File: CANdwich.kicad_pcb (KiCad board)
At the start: 2 copper layers, 43 parts, among them J1 DE9_Receptacle, J2 USB_C_Receptacle_USB2.0, J3 Conn_02x05_Odd_Even, J4 Conn_01x04_Socket, U1 AP2127K-3.3, U2 STM32F072CBT6, U3 SN6505BDBV, U5 AP2204RA-5.0, U6 ISO1050DUB, Y1 16MHz

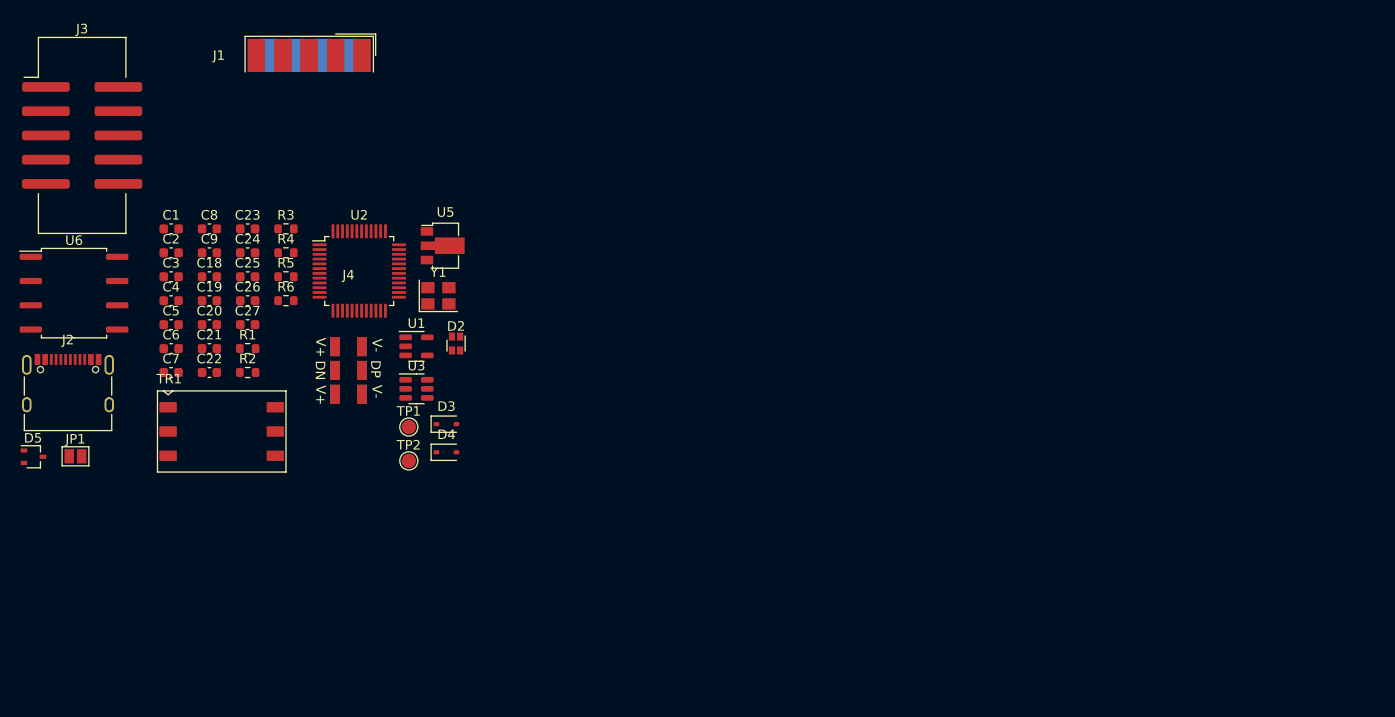
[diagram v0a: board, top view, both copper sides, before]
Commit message: Placement in KICAD V7.0.5
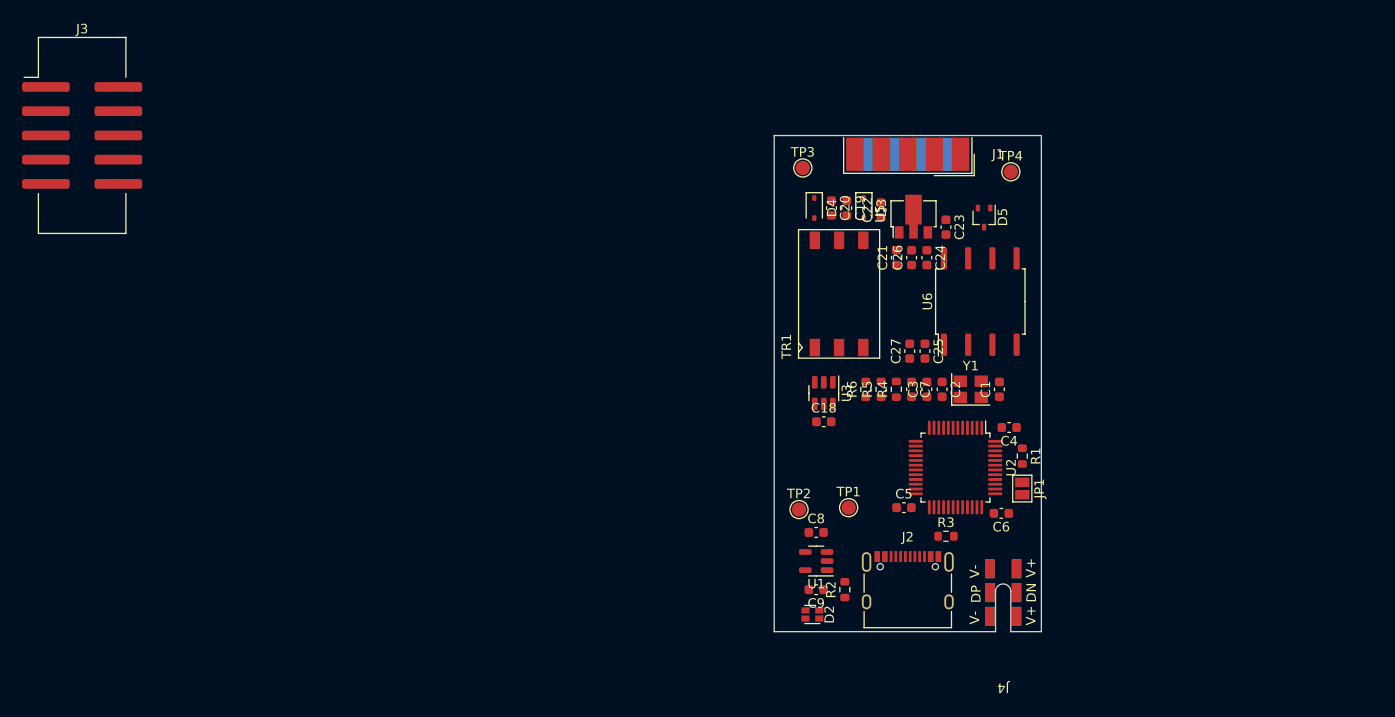
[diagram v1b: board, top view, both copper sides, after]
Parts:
- added TP3: TestPoint, TestPoint:TestPoint_Pad_D1.5mm, F.Cu at (119.0, 60.4)
- added TP4: TestPoint, TestPoint:TestPoint_Pad_D1.5mm, F.Cu at (140.8, 60.8)
- J1: footprint Connector_Dsub:DSUB-9_Female_EdgeMount_P2.77mm -> Connector_Dsub:DSUB-9_Male_EdgeMount_P2.77mm
- moved D5 102.7 mm to (138.0, 65.6), turned to -90 degrees
- moved JP1 99.3 mm to (142.0, 94.0), turned to -90 degrees
- moved U6 95.0 mm to (137.6, 74.4), turned to 90 degrees
- moved J2 90.4 mm to (130.0, 104.8)
- moved C4 88.8 mm to (140.6, 87.6), turned to 180 degrees
- moved C6 88.7 mm to (139.8, 96.6), turned to 180 degrees
- moved C1 88.4 mm to (139.6, 83.6), turned to 90 degrees
- moved C2 82.1 mm to (133.6, 83.6), turned to -90 degrees
- moved R1 82.0 mm to (142.0, 90.6), turned to -90 degrees
- moved C3 80.1 mm to (132.0, 83.6), turned to 90 degrees
- moved C5 79.2 mm to (129.6, 96.0)
- moved C7 77.6 mm to (130.4, 83.6), turned to -90 degrees
- moved R3 76.3 mm to (134.0, 99.0)
- moved J4 75.4 mm to (140.0, 108.9), turned to 180 degrees
- moved C23 73.2 mm to (134.0, 66.6), turned to -90 degrees
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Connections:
- TR1 pad 1: Net-(U3-D1) -> Net-(U3-D2)
- TR1 pad 3: Net-(U3-D2) -> Net-(U3-D1)
- TR1 pad 4: Net-(D4-A) -> Net-(D3-A)
- TR1 pad 6: Net-(D3-A) -> Net-(D4-A)
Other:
- board outline added: 28 x 52 mm

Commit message: Snapshot for layout
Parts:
- removed C21: 1u, Capacitor_SMD:C_0603_1608Metric
- removed J3: Conn_02x05_Odd_Even, Connector_IDC:IDC-Header_2x05_P2.54mm_Vertical_SMD
- removed JP1: Jumper_2_Open, Jumper:SolderJumper-2_P1.3mm_Open_Pad1.0x1.5mm
- added R7: 150, Resistor_SMD:R_0603_1608Metric, F.Cu at (135.6, 97.6)
- added TP5: TestPoint, TestPoint:TestPoint_Pad_D1.5mm, F.Cu at (140.0, 95.4)
- added TP6: TestPoint, TestPoint:TestPoint_Pad_D1.5mm, F.Cu at (140.0, 97.9)
- added TP7: TestPoint, TestPoint:TestPoint_Pad_D1.5mm, F.Cu at (140.0, 92.9)
- added TP8: TestPoint, TestPoint:TestPoint_Pad_D1.5mm, F.Cu at (139.0, 69.9)
- added TP9: TestPoint, TestPoint:TestPoint_Pad_D1.5mm, F.Cu at (140.0, 90.4)
- R4, R5, R6: value 121 -> 150
- Y1: footprint Crystal:Crystal_SMD_3225-4Pin_3.2x2.5mm -> Crystal:Crystal_SMD_2520-4Pin_2.5x2.0mm
- moved R6 22.0 mm to (119.4, 104.7)
- moved R1 7.50 mm to (136.0, 95.1)
- moved C8 7.25 mm to (123.8, 105.0), turned to 90 degrees
- moved C4 6.72 mm to (134.8, 91.0)
- moved U2 6.36 mm to (129.5, 95.0)
- moved C5 6.13 mm to (123.5, 96.6), turned to -90 degrees
- moved TP3 5.85 mm to (121.0, 65.9)
- moved D5 5.76 mm to (136.2, 71.0)
- moved C6 5.73 mm to (134.8, 99.4)
- moved C1 5.66 mm to (135.6, 87.6)
- moved TP4 5.41 mm to (139.0, 65.9)
- moved R2 5.36 mm to (124.2, 99.3), turned to 180 degrees
- moved Y1 5.32 mm to (133.1, 87.6)
- moved D4 5.01 mm to (121.0, 69.5)
- moved C2 5.00 mm to (130.6, 87.6)
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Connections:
- net /USB_DM renamed /USB_D-
- net /USB_DP renamed /USB_D+
- net Net-(U2-PF0) renamed /clk_P
- net Net-(U2-PF1) renamed /clk_N
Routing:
- net Net-(D2-RK): track 0.00 -> 31.8 mm, vias 0 -> 2
- net Net-(D2-GK): track 0.00 -> 28.2 mm, vias 0 -> 2
- net VBUS: track 0.00 -> 24.9 mm, vias 0 -> 13
- net /USB_D-: track 0.00 -> 24.1 mm, vias 0 -> 2
- net /USB_D+: track 0.00 -> 21.9 mm, vias 0 -> 2
- net /CAN_RX: track 0.00 -> 18.8 mm
- net +5VD: track 0.00 -> 17.9 mm, vias 0 -> 2
- net /nRST: track 0.00 -> 14.9 mm, vias 0 -> 2
- net /SWDIO: track 0.00 -> 14.3 mm, vias 0 -> 2
- net /CAN_TX: track 0.00 -> 12.4 mm
- net /CANH: track 0.00 -> 11.8 mm, vias 0 -> 1
- net /CANL: track 0.00 -> 11.8 mm
- net Earth: track 0.00 -> 11.2 mm, vias 0 -> 44
- net /SWCLK: track 0.00 -> 9.21 mm, vias 0 -> 2
- net VD3V3: track 0.00 -> 8.86 mm
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- added copper zone on B.Cu, net +12V
- added copper zone on F.Cu, net +12V
- added copper zone on B.Cu, net Earth
- added copper zone on F.Cu, net Earth
- added copper zone on B.Cu, net GNDA
- added copper zone on F.Cu, net GNDA
- added copper zone on B.Cu, net VBUS
- added copper zone on F.Cu, net VBUS
- added copper zone on F.Cu, net VD3V3
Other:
- board size 28 x 52 mm -> 26 x 46 mm

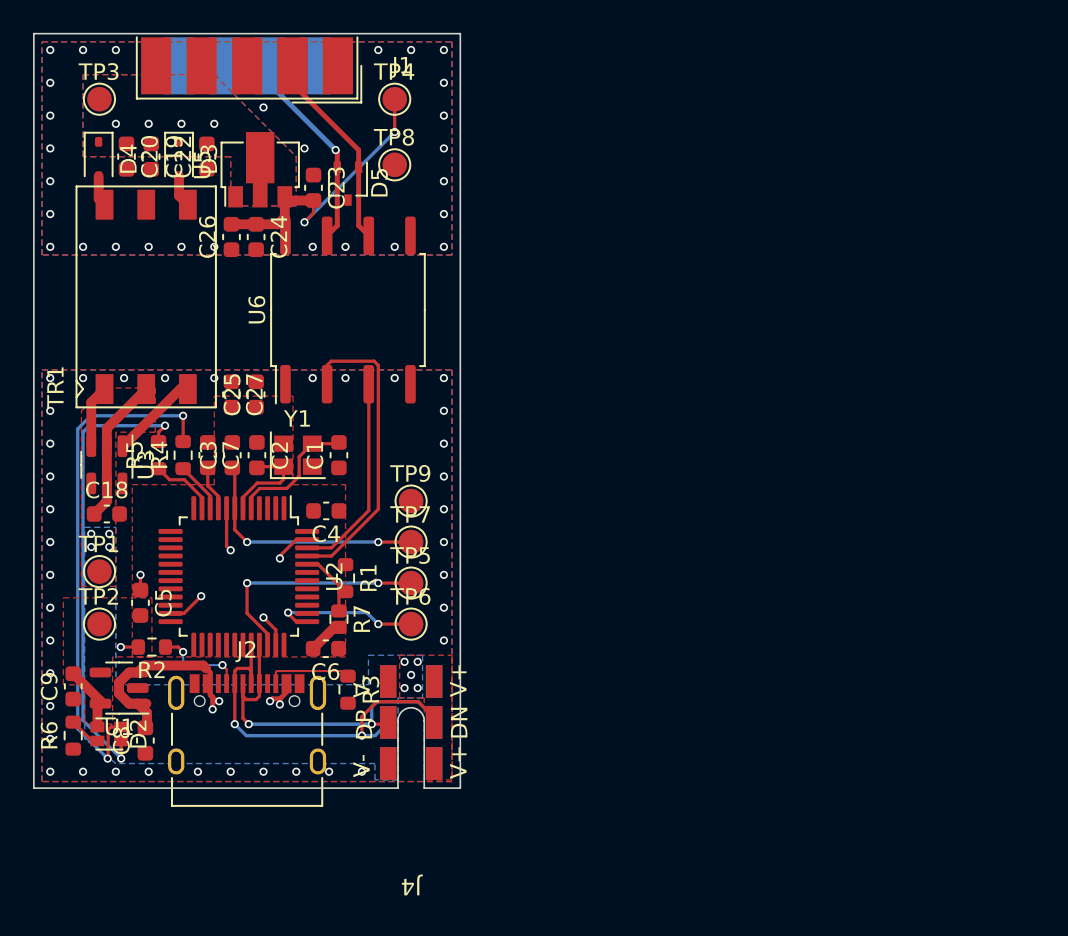
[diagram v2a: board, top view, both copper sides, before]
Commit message: resize edge.cuts
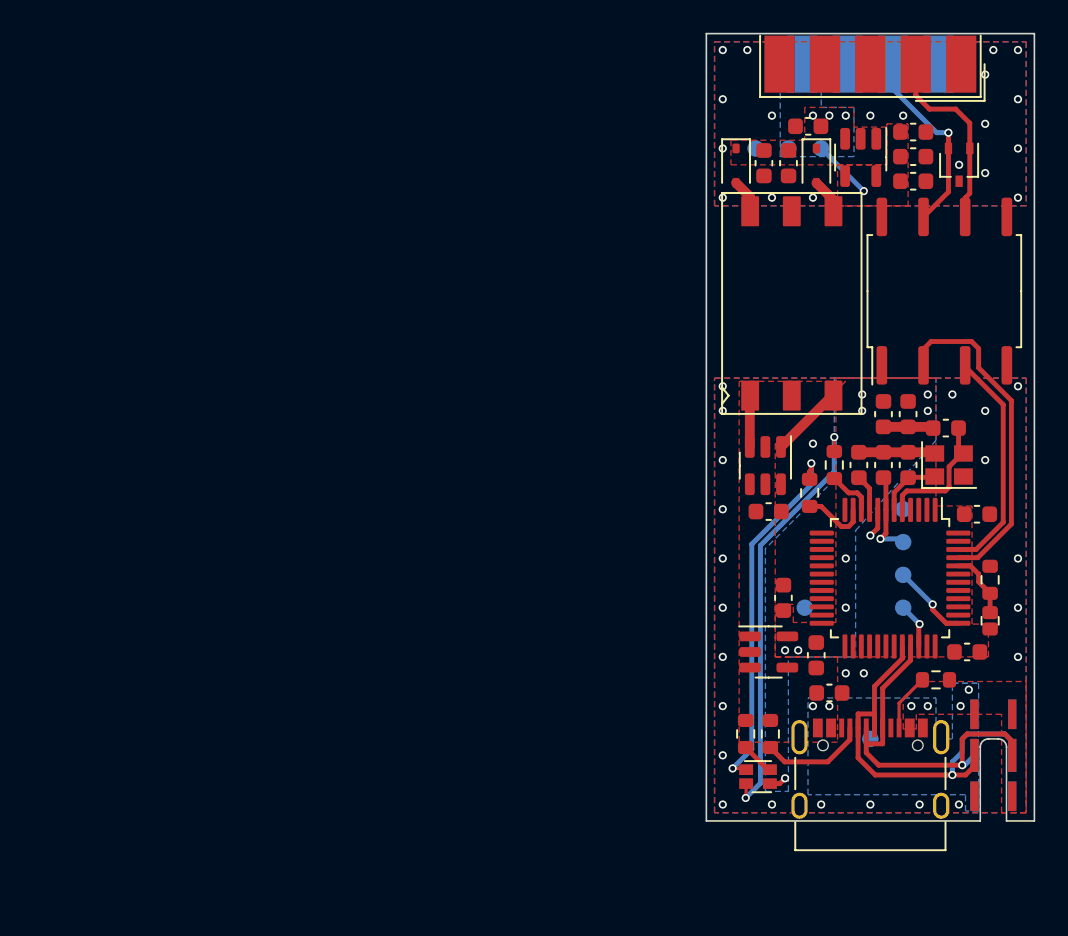
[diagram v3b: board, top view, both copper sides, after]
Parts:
- removed U5: AP2204RA-5.0, Package_TO_SOT_SMD:SOT-89-3
- added G***: LOGO, LOGO, B.Cu at (230.3, 72.2)
- added U4: AP2204K-5.0TRG1, Package_TO_SOT_SMD:SOT-23-5, F.Cu at (167.4, 69.5)
- J4: moved to B.Cu
- TP1, TP2, TP3, TP4, TP5, TP6, TP7, TP8, TP9: footprint TestPoint:TestPoint_Pad_D1.5mm -> TestPoint:TestPoint_Pad_D1.0mm; moved to B.Cu
- moved TP1 48.1 mm to (168.0, 104.9), turned to 180 degrees
- moved C9 43.6 mm to (162.7, 96.3), turned to -90 degrees
- moved TP2 43.0 mm to (164.0, 96.9), turned to 180 degrees
- moved TP3 42.1 mm to (163.0, 68.9), turned to 180 degrees
- moved C26 41.8 mm to (170.6, 69.4), turned to 180 degrees
- moved C8 41.8 mm to (165.5, 102.1), turned to 180 degrees
- moved C5 41.3 mm to (164.7, 99.8), turned to 90 degrees
- moved C27 41.3 mm to (170.3, 85.1), turned to 90 degrees
- moved R6 41.0 mm to (160.4, 104.6), turned to -90 degrees
- moved C24 40.6 mm to (170.6, 67.9), turned to 0 degrees
- moved C18 40.4 mm to (161.8, 91.0)
- moved U3 40.2 mm to (161.6, 88.2)
- moved R5 39.8 mm to (164.3, 89.9)
- moved C2 39.7 mm to (170.3, 88.2)
- moved C3 39.7 mm to (168.8, 88.2)
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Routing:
- net VBUS: track 24.9 -> 0.00 mm, vias 13 -> 6
- net +5VD: track 17.9 -> 3.68 mm, vias 2 -> 1
- net /SWDIO: track 14.3 -> 2.80 mm, vias 2 -> 1
- net /nRST: track 14.9 -> 5.40 mm, vias 2 -> 1
- net Net-(D2-RK): track 31.8 -> 26.0 mm
- net Net-(D2-GK): track 28.2 -> 22.5 mm
- net VD3V3: track 8.86 -> 3.29 mm, vias 0 -> 9
- net /SWCLK: track 9.21 -> 4.77 mm, vias 2 -> 1
- net /clk_N: track 6.03 -> 3.92 mm
- net Net-(J2-CC2): track 5.26 -> 3.52 mm
- net Earth: track 11.2 -> 9.46 mm, vias 44 -> 26
- net /CAN_RX: track 18.8 -> 20.3 mm
- net /CAN_TX: track 12.4 -> 14.0 mm
- net /USB_D-: track 24.1 -> 25.3 mm, vias 2 -> 1
- net Net-(J2-CC1): track 5.52 -> 6.49 mm, vias 2 -> 0
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- added copper zone on F.Cu, net +5VD
- added copper zone on B.Cu, net VD3V3
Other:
- board size 26 x 46 mm -> 20 x 48 mm

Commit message: V1.0 Generate external enclosure
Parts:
- moved G*** 63.9 mm to (168.0, 86.2)

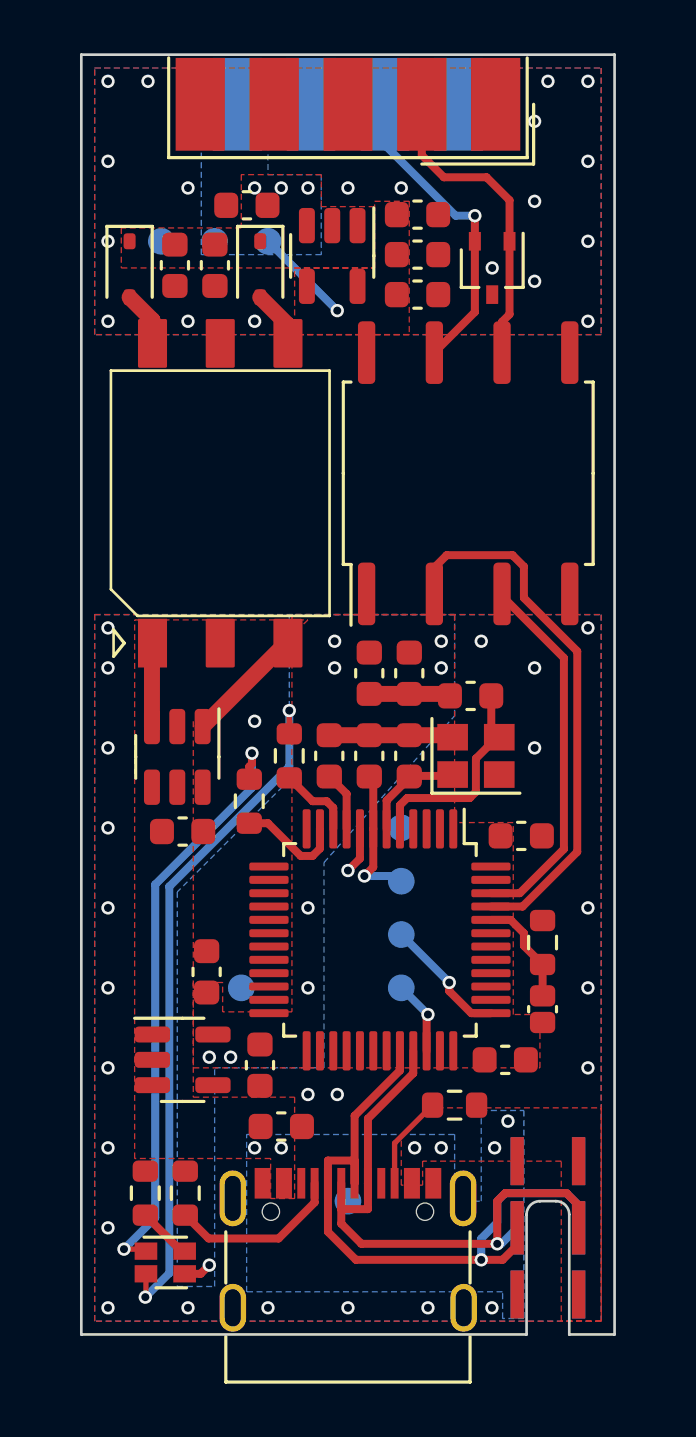
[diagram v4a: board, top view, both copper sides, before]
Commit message: Change USB edge connection interface
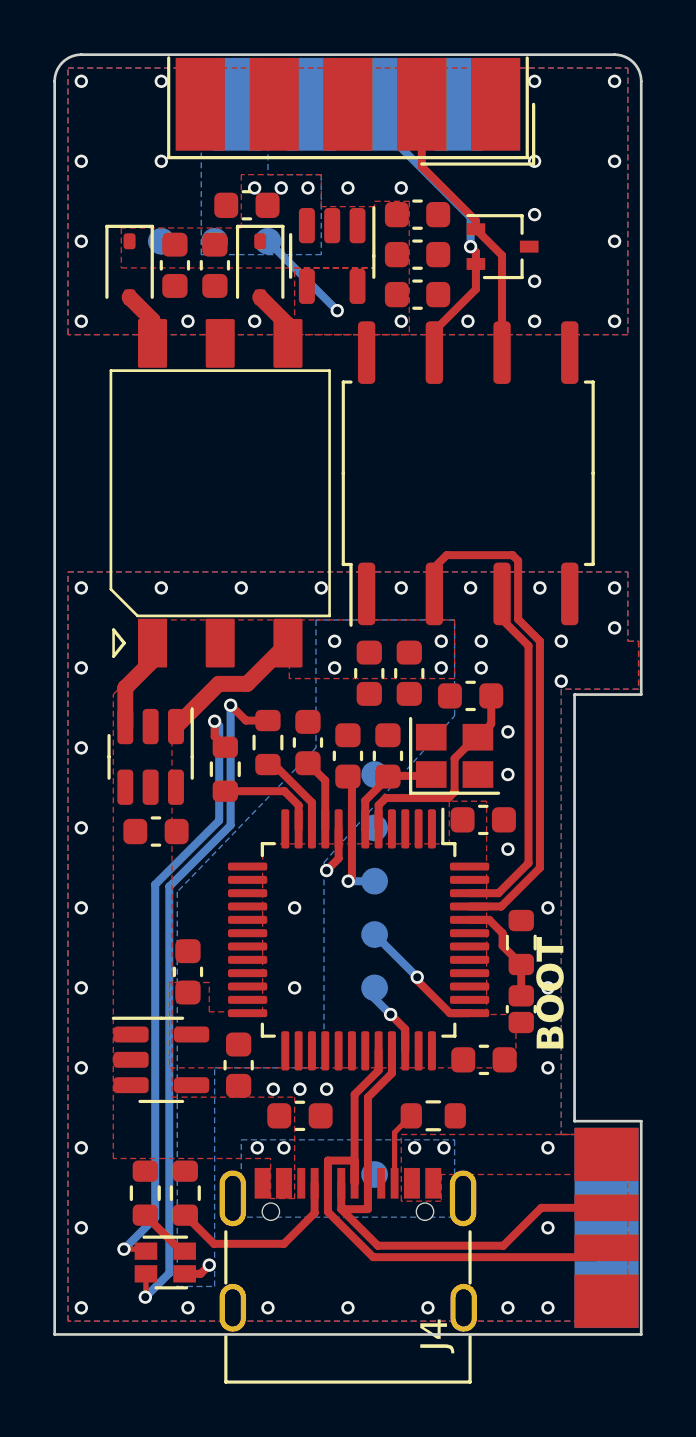
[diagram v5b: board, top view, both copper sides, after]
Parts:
- J4: footprint 0_terry:USB_snowflake -> 0_terry:USB_EdgeMount; moved to F.Cu
- moved TP2 9.43 mm to (169.0, 88.9)
- moved G*** 4.14 mm to (166.5, 90.1)
- moved C4 1.55 mm to (173.1, 90.6)
- moved R5 1.50 mm to (163.4, 88.7)
- moved TP1 1.41 mm to (169.0, 103.9)
- moved C18 1.00 mm to (160.8, 91.0)
- moved J4 1.00 mm to (176.5, 109.9), turned to 90 degrees
- moved TP5 1.00 mm to (169.0, 96.9)
- moved TP6 1.00 mm to (169.0, 94.9)
- moved TP7 1.00 mm to (169.0, 92.9)
- moved TP9 1.00 mm to (169.0, 90.9)
- moved U3 1.00 mm to (160.6, 88.2)
- moved C7 0.94 mm to (166.5, 87.7)
- moved R4 0.94 mm to (165.0, 87.7)
- moved R3 0.89 mm to (171.2, 101.7)
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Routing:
- net Earth: track 9.46 -> 1.75 mm, vias 26 -> 40
- net /USB_D-: track 25.3 -> 20.5 mm, vias 1 -> 0
- net /USB_D+: track 22.1 -> 19.4 mm, vias 1 -> 0
- net /CANL: track 11.7 -> 10.6 mm
- net Net-(U3-D1): track 4.50 -> 5.50 mm
- net Net-(D2-GK): track 22.5 -> 23.3 mm
- net /CAN_RX: track 20.3 -> 19.5 mm
- net /CAN_TX: track 14.0 -> 13.2 mm
- net Net-(J2-CC2): track 3.52 -> 2.79 mm
- net VD3V3: track 3.29 -> 3.79 mm, vias 9 -> 7
- net VBUS: vias 6 -> 4
- net GNDA: vias 19 -> 21
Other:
- board size 20 x 48 mm -> 22 x 48 mm
- board text added: "0V"
- board text added: "12V"
- board text added: "3V3"
- board text added: "5V"
- board text added: "BOOT"
- board text added: "CLK"
- board text added: "DIO"
- board text added: "GND"
- board text added: "RST"
- board text added: "VBUS"
